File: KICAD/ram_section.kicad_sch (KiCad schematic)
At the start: 6 parts, among them U1 HY5117404B, U2 HY5117404B

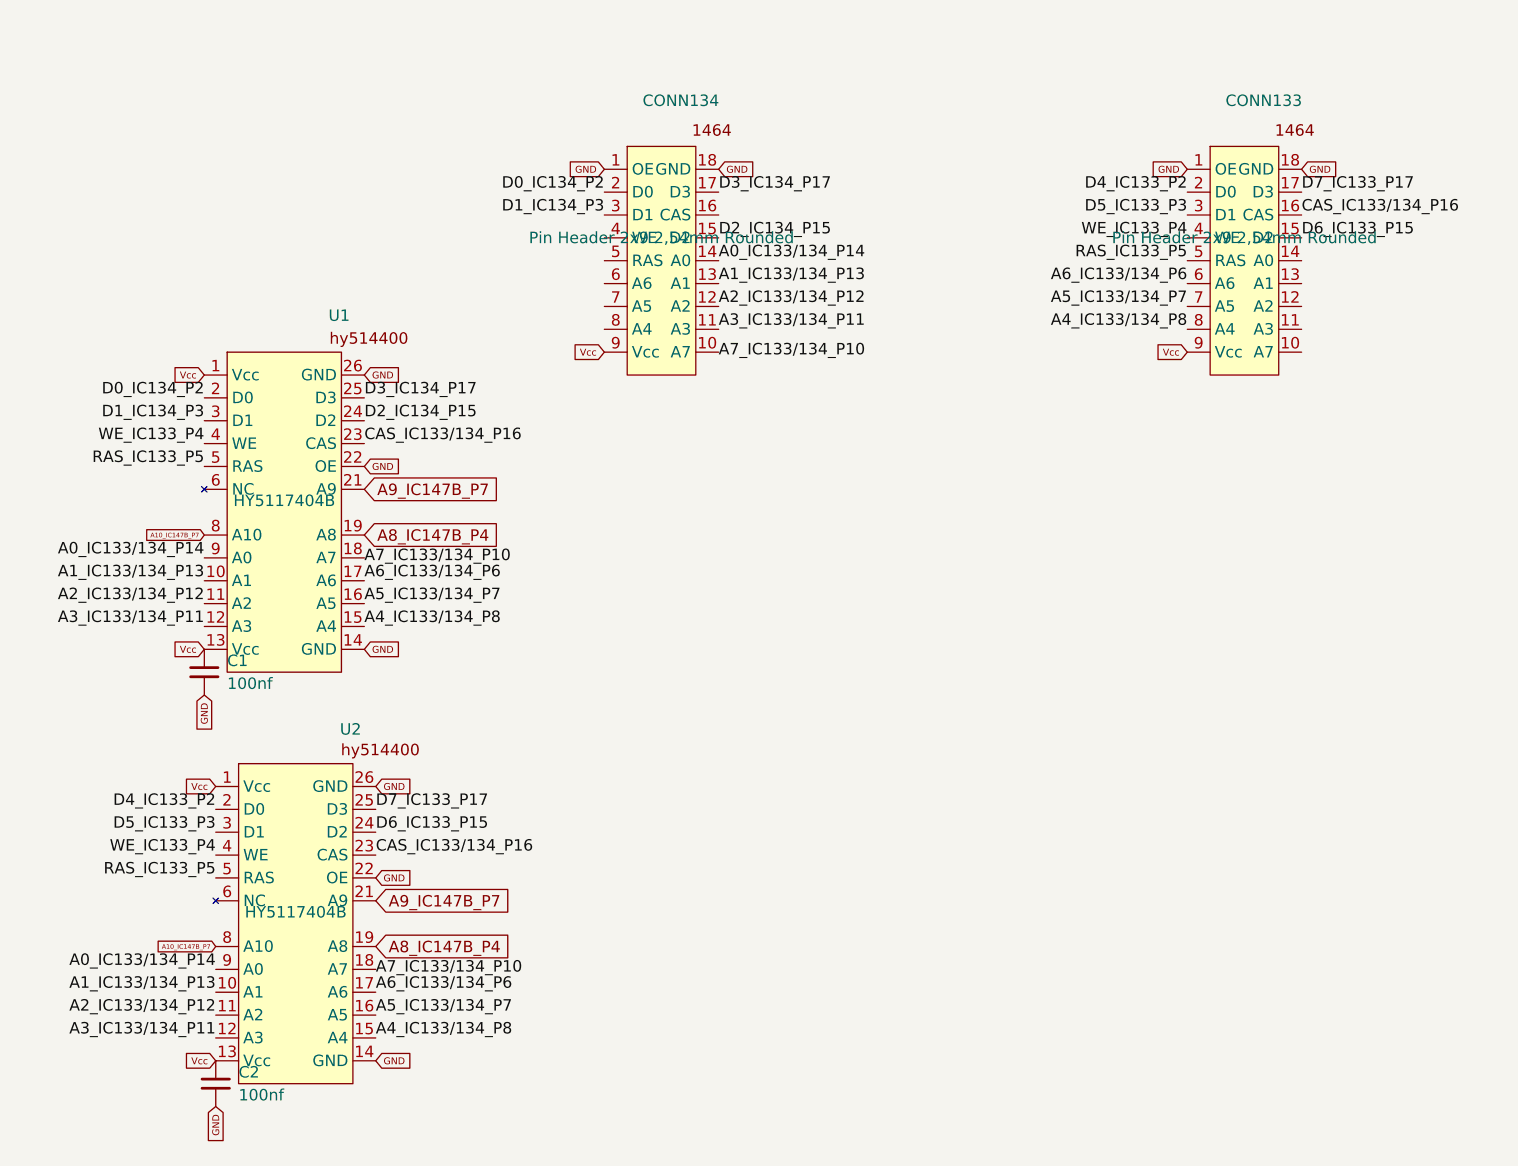
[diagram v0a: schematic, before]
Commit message: Publish 4 MB mapper project
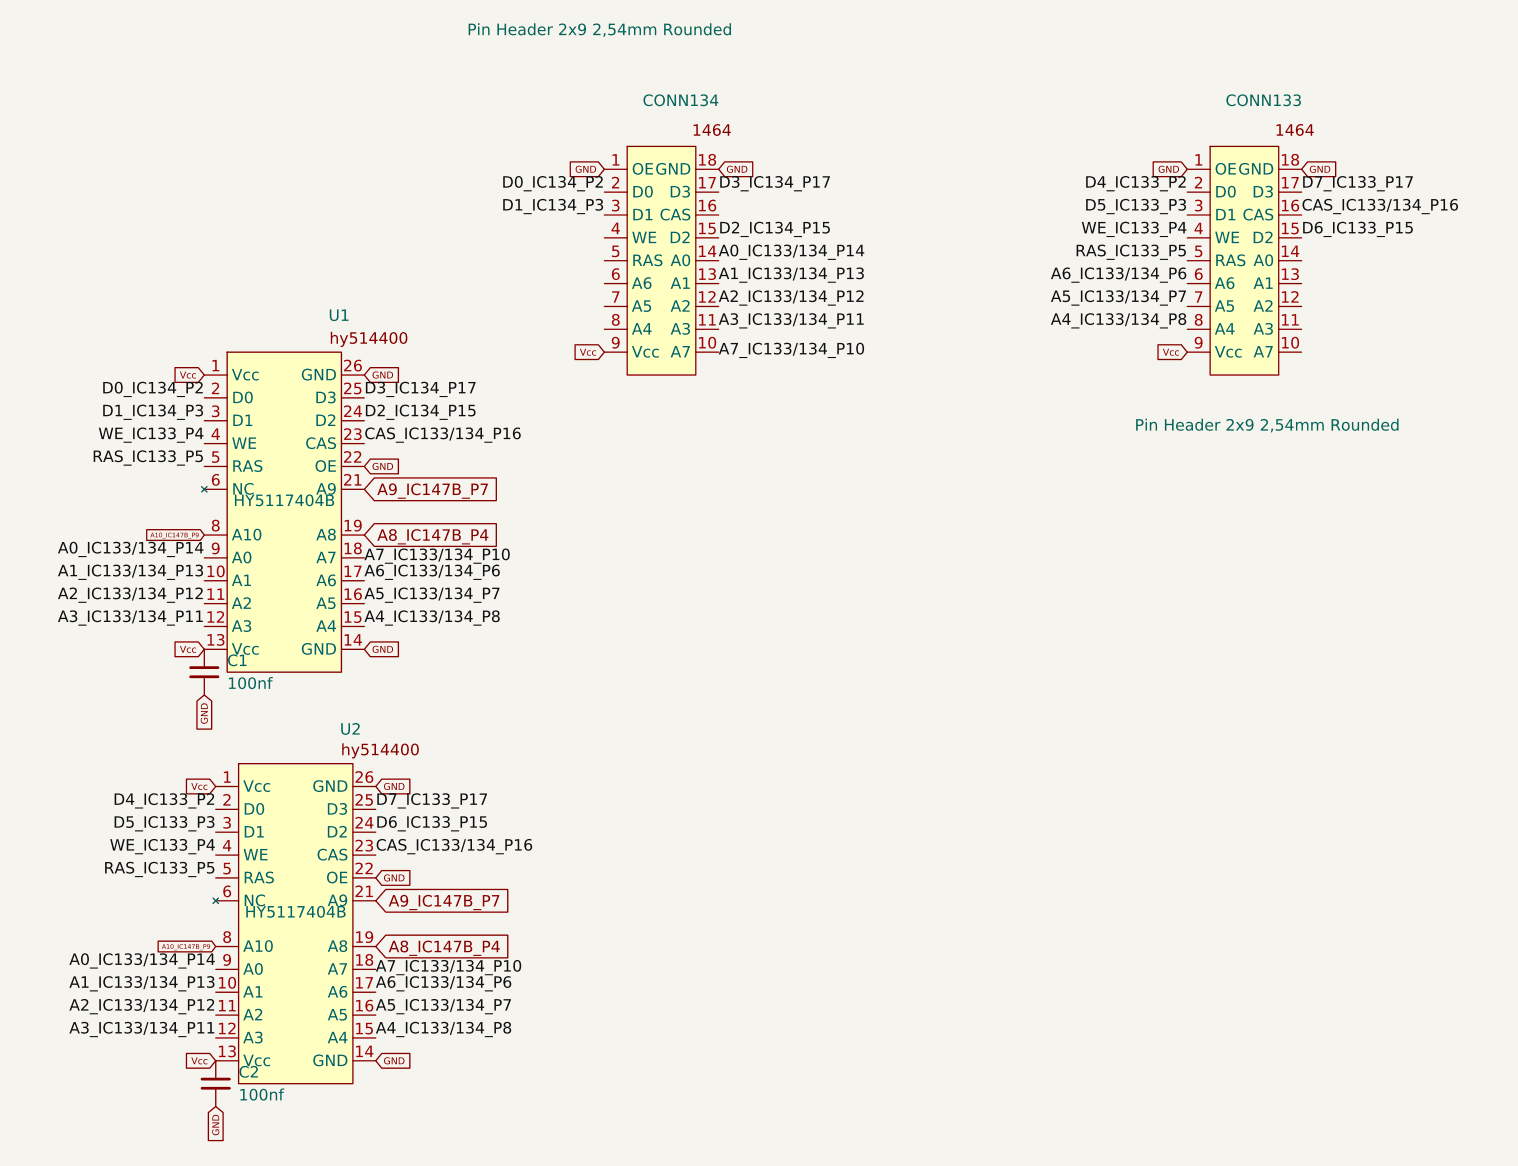
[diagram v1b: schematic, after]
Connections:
- net A10_IC147B_P7 renamed A10_IC147B_P9
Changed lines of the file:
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@@
 		)
 	)
-	(global_label "A10_IC147B_P7"
+	(global_label "A10_IC147B_P9"
 		(shape input)
 		(at 68.58 86.36 180)
@@
 		)
 	)
-	(global_label "A10_IC147B_P7"
+	(global_label "A10_IC147B_P9"
 		(shape input)
 		(at 69.85 132.08 180)
@@
 		(in_pos_files yes)
 		(dnp no)
-		(fields_autoplaced yes)
 		(property "Reference" "CONN133"
 			(at 186.3041 38.1 0)
@@
 		)
 		(property "Value" "Pin Header 2x9 2,54mm Rounded"
-			(at 184.15 53.34 0)
+			(at 186.69 74.168 0)
 			(show_name no)
 			(do_not_autoplace no)
@@
 		(in_pos_files yes)
 		(dnp no)
-		(fields_autoplaced yes)
 		(property "Reference" "CONN134"
 			(at 121.5341 38.1 0)
@@
 		)
 		(property "Value" "Pin Header 2x9 2,54mm Rounded"
-			(at 119.38 53.34 0)
+			(at 112.522 30.226 0)
 			(show_name no)
 			(do_not_autoplace no)
@@
 		)
 	)
+	(embedded_fonts no)
 )
